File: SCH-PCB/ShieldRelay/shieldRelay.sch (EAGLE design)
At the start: 56 parts, among them IC1 LM2596SX-5.0_NOPB, K1 SLA-05VDC-SL-C, K2 SRD-05VDC-SL-C, K3 G3MB-202PL-DC5, K5 G3MB-202PL-DC5, K6 SRD-05VDC-SL-C, Q1 MMST2222A-7-F, Q2 MMST2222A-7-F, Q3 MMST2222A-7-F, Q4 MMST2222A-7-F, Q5 MMST2222A-7-F

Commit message: FEAT: update schematic
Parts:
- added GND: (no value), pinhead:PINHD-2X4
- added JP13: (no value), pinhead_mod:PINHD-1X15
- renumbered JP10 to VIN, JP7 to VCC_SELECT, JP8 to VCC, JP9 to GND_
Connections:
- net GND: now also GND.1, GND.2, GND.3, GND.4, GND.5, GND.6, GND.7, GND.8
- net N$17: now also JP13.1
- net N$19: now also JP13.2
- net N$20: now also JP13.3
- net N$21: now also JP13.4
- net N$22: now also JP13.5
- net N$28: now also JP13.6
- net N$29: now also JP13.7
- net N$30: now also JP13.8
- net N$31: now also JP13.9
- net N$32: now also JP13.10
- net N$33: now also JP13.11
- net N$34: now also JP13.12
- net N$35: now also JP13.13
- net N$36: now also JP13.14
- net N$37: now also JP13.15

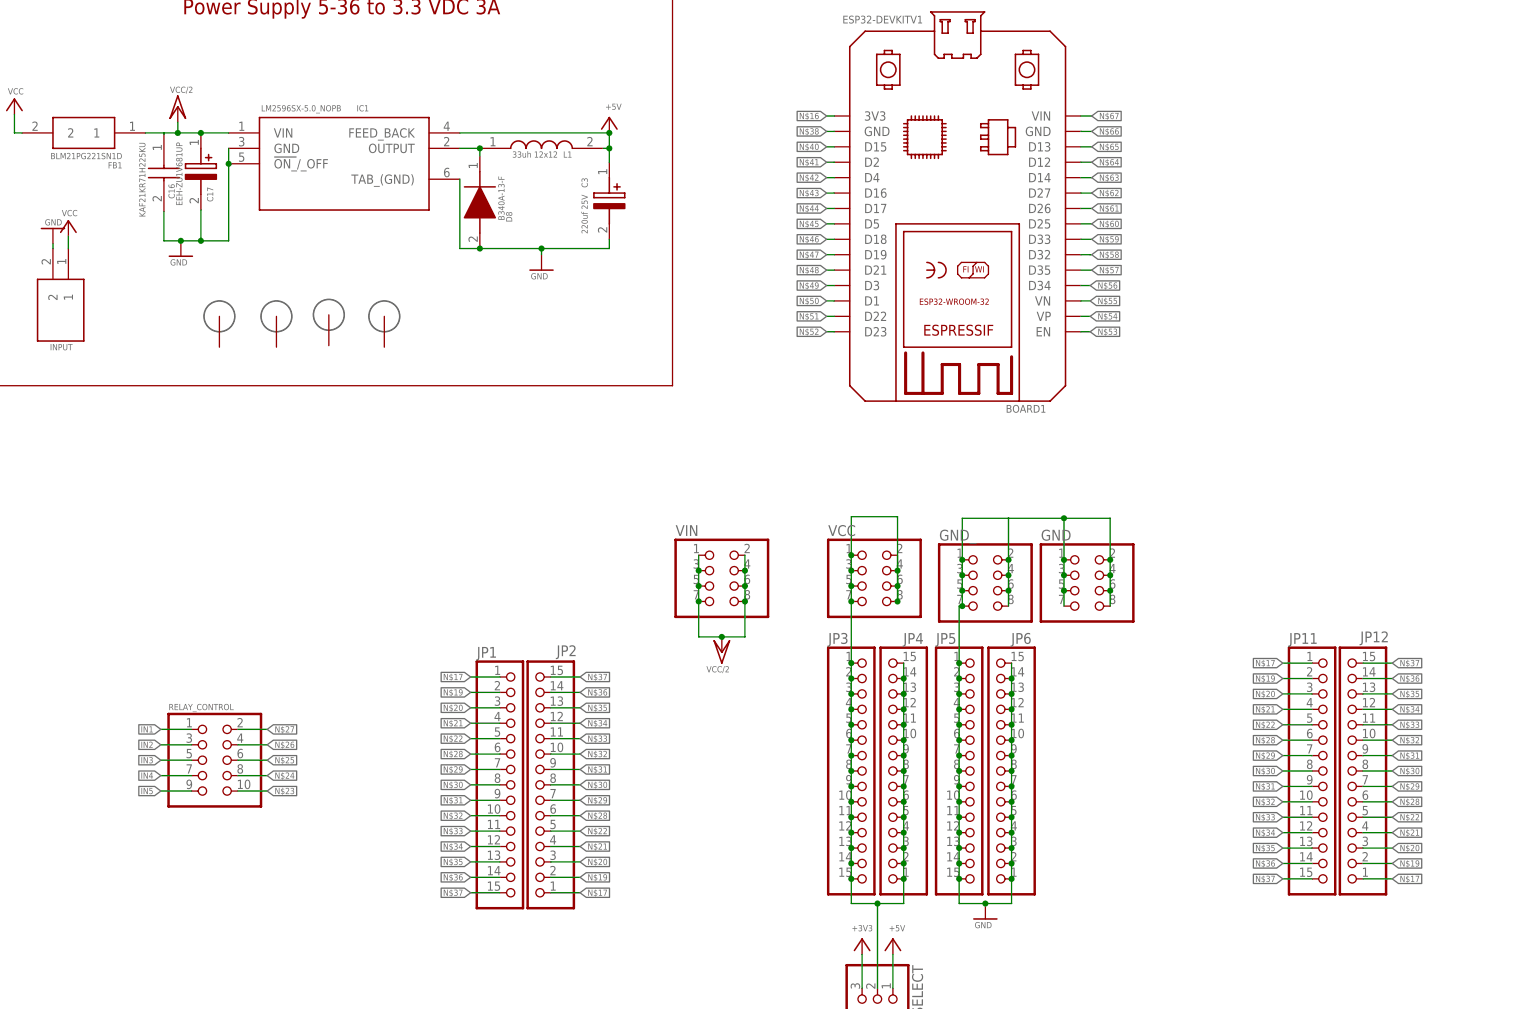
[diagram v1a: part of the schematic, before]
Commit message: FEAT: add 3v3 regulator
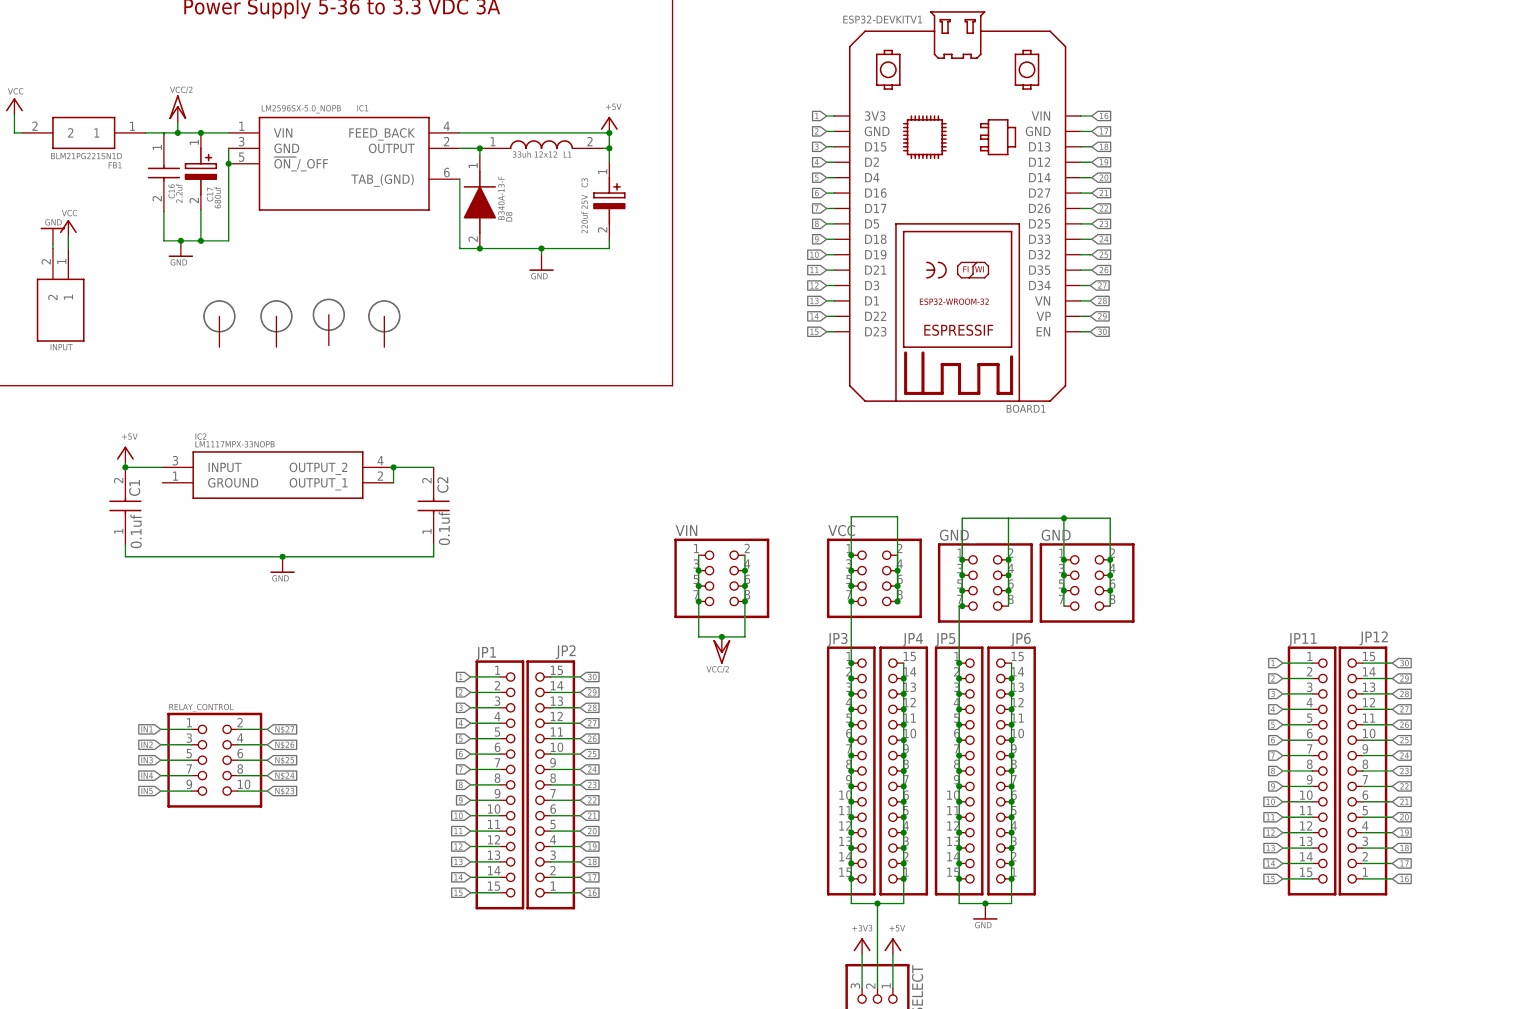
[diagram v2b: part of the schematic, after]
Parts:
- added C1, C2: 0.1uf, KGM15BR71E104KT:KGM15BR71E104KT
- added IC2: LM1117MPX-33NOPB, LM1117MPX-33NOPB:LM1117MPX-33NOPB
- C16: value KAF21KR71H225KU -> 2.2uf
- C17: value EEH-ZU1V681UP -> 680uf
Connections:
- removed net N$16: BOARD1.3V3
- removed net N$40: BOARD1.D15
- removed net N$41: BOARD1.D2
- removed net N$42: BOARD1.D4
- removed net N$43: BOARD1.D16
- removed net N$44: BOARD1.D17
- removed net N$45: BOARD1.D5
- removed net N$46: BOARD1.D18
- removed net N$47: BOARD1.D19
- removed net N$48: BOARD1.D21
- removed net N$49: BOARD1.D3
- removed net N$50: BOARD1.D1
- removed net N$51: BOARD1.D22
- removed net N$52: BOARD1.D23
- removed net N$53: BOARD1.EN
- removed net N$54: BOARD1.VP
- removed net N$55: BOARD1.VN
- removed net N$56: BOARD1.D34
- removed net N$57: BOARD1.D35
- removed net N$58: BOARD1.D32
- removed net N$59: BOARD1.D33
- removed net N$60: BOARD1.D25
- removed net N$61: BOARD1.D26
- removed net N$62: BOARD1.D27
- removed net N$63: BOARD1.D14
- removed net N$64: BOARD1.D12
- removed net N$65: BOARD1.D13
- removed net N$66: BOARD1.GND
- removed net N$67: BOARD1.VIN
- new net 1: BOARD1.3V3, JP1.1, JP11.1
- new net 10: BOARD1.D19, JP1.10, JP11.10
- new net 11: BOARD1.D21, JP1.11, JP11.11
- new net 12: BOARD1.D3, JP1.12, JP11.12
- new net 13: BOARD1.D1, JP1.13, JP11.13
- new net 14: BOARD1.D22, JP1.14, JP11.14
- new net 15: BOARD1.D23, JP1.15, JP11.15
- new net 16: BOARD1.VIN, JP12.1, JP2.1
- new net 17: BOARD1.GND, JP12.2, JP2.2
- new net 18: BOARD1.D13, JP12.3, JP2.3
- new net 19: BOARD1.D12, JP12.4, JP2.4
- new net 2: BOARD1.GND@1, JP1.2, JP11.2
- new net 20: BOARD1.D14, JP12.5, JP2.5
- new net 21: BOARD1.D27, JP12.6, JP2.6
- new net 22: BOARD1.D26, JP12.7, JP2.7
- new net 23: BOARD1.D25, JP12.8, JP2.8
- new net 24: BOARD1.D33, JP12.9, JP2.9
- new net 25: BOARD1.D32, JP12.10, JP2.10
- new net 26: BOARD1.D35, JP12.11, JP2.11
- new net 27: BOARD1.D34, JP12.12, JP2.12
- new net 28: BOARD1.VN, JP12.13, JP2.13
- new net 29: BOARD1.VP, JP12.14, JP2.14
- new net 3: BOARD1.D15, JP1.3, JP11.3
- new net 30: BOARD1.EN, JP12.15, JP2.15
- new net 4: BOARD1.D2, JP1.4, JP11.4
- new net 5: BOARD1.D4, JP1.5, JP11.5
- new net 6: BOARD1.D16, JP1.6, JP11.6
- new net 7: BOARD1.D17, JP1.7, JP11.7
- new net 8: BOARD1.D5, JP1.8, JP11.8
- new net 9: BOARD1.D18, JP1.9, JP11.9
- net +5V: now also C1.2, IC2.INPUT
- net GND: now also C1.1, C2.1
- net N$17: no longer JP1.1, JP11.1, JP12.1, JP2.1
- net N$19: no longer JP1.2, JP11.2, JP12.2, JP2.2
- net N$20: no longer JP1.3, JP11.3, JP12.3, JP2.3
- net N$21: no longer JP1.4, JP11.4, JP12.4, JP2.4
- net N$22: no longer JP1.5, JP11.5, JP12.5, JP2.5
- net N$28: no longer JP1.6, JP11.6, JP12.6, JP2.6
- net N$29: no longer JP1.7, JP11.7, JP12.7, JP2.7
- net N$30: no longer JP1.8, JP11.8, JP12.8, JP2.8
- net N$31: no longer JP1.9, JP11.9, JP12.9, JP2.9
- net N$32: no longer JP1.10, JP11.10, JP12.10, JP2.10
- net N$33: no longer JP1.11, JP11.11, JP12.11, JP2.11
- net N$34: no longer JP1.12, JP11.12, JP12.12, JP2.12
- net N$35: no longer JP1.13, JP11.13, JP12.13, JP2.13
- net N$36: no longer JP1.14, JP11.14, JP12.14, JP2.14
- net N$37: no longer JP1.15, JP11.15, JP12.15, JP2.15
- net N$38: now also C2.2, IC2.OUTPUT_1, IC2.OUTPUT_2; no longer BOARD1.GND@1

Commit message: FEAT: update board
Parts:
- renumbered BOARD1 to BOARD, GND to GND_1, GND_ to GND_2, LED1 to RL3, LED2 to RL1, LED3 to RL4, LED4 to RL5, LED6 to RL2

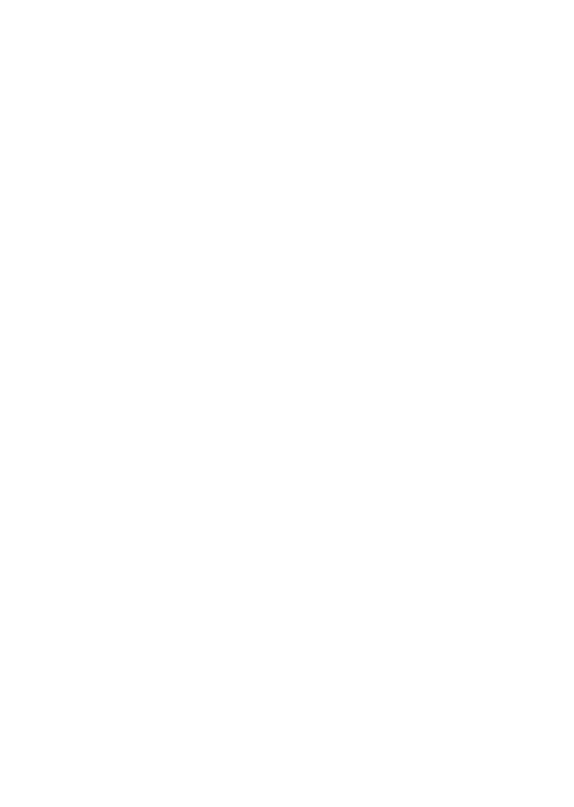
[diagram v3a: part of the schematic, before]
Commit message: FEAT: update terminal block
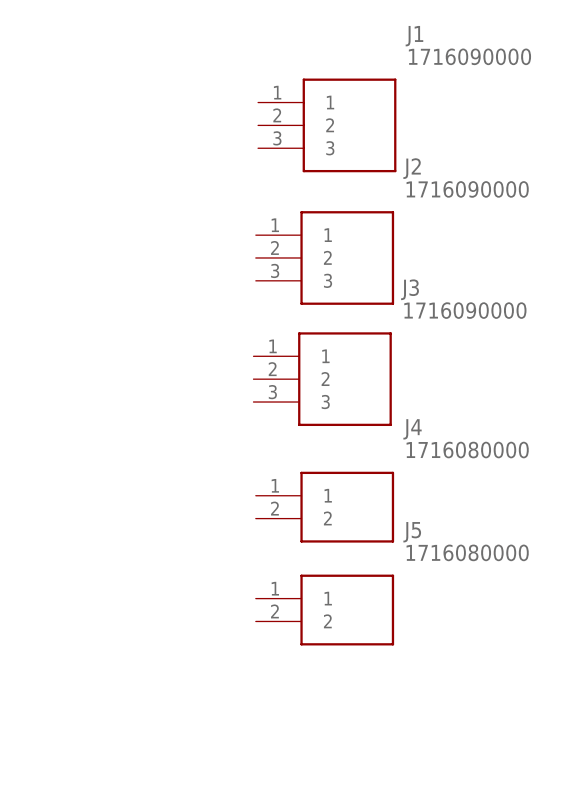
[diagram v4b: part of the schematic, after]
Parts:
- added J1, J2, J3: 1716090000, 1716090000:1716090000
- added J4, J5: 1716080000, 1716080000:1716080000
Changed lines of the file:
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@@
 <part name="GND10" library="supply1" library_urn="urn:adsk.eagle:library:371" deviceset="GND" device=""/>
 <part name="P+12" library="supply1" library_urn="urn:adsk.eagle:library:371" deviceset="+5V" device=""/>
+<part name="J1" library="1716090000" deviceset="1716090000" device=""/>
+<part name="J2" library="1716090000" deviceset="1716090000" device=""/>
+<part name="J3" library="1716090000" deviceset="1716090000" device=""/>
+<part name="J4" library="1716080000" deviceset="1716080000" device=""/>
+<part name="J5" library="1716080000" deviceset="1716080000" device=""/>
 </parts>
 <sheets>
@@
 <attribute name="VALUE" x="300.99" y="105.664" size="1.016" layer="96" rot="R180"/>
 </instance>
+<instance part="J1" gate="G$1" x="526.542" y="176.022" smashed="yes">
+<attribute name="NAME" x="543.052" y="183.642" size="1.778" layer="95" align="center-left"/>
+<attribute name="VALUE" x="543.052" y="181.102" size="1.778" layer="96" align="center-left"/>
+</instance>
+<instance part="J2" gate="G$1" x="526.288" y="161.29" smashed="yes">
+<attribute name="NAME" x="542.798" y="168.91" size="1.778" layer="95" align="center-left"/>
+<attribute name="VALUE" x="542.798" y="166.37" size="1.778" layer="96" align="center-left"/>
+</instance>
+<instance part="J3" gate="G$1" x="526.034" y="147.828" smashed="yes">
+<attribute name="NAME" x="542.544" y="155.448" size="1.778" layer="95" align="center-left"/>
+<attribute name="VALUE" x="542.544" y="152.908" size="1.778" layer="96" align="center-left"/>
+</instance>
+<instance part="J4" gate="G$1" x="526.288" y="132.334" smashed="yes">
+<attribute name="NAME" x="542.798" y="139.954" size="1.778" layer="95" align="center-left"/>
+<attribute name="VALUE" x="542.798" y="137.414" size="1.778" layer="96" align="center-left"/>
+</instance>
+<instance part="J5" gate="G$1" x="526.288" y="120.904" smashed="yes">
+<attribute name="NAME" x="542.798" y="128.524" size="1.778" layer="95" align="center-left"/>
+<attribute name="VALUE" x="542.798" y="125.984" size="1.778" layer="96" align="center-left"/>
+</instance>
 </instances>

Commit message: DOC: UPDATE SCHEMATIC, BOARD AND ADD PDF
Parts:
- removed J1, J2, J3: 1716090000, 1716090000:1716090000
- removed J4, J5: 1716080000, 1716080000:1716080000
- removed JP1, JP2, JP3, JP4, JP5, JP6: (no value), pinhead_mod:PINHD-1X15
- added GND_3, GND_4, SIGNAL_3, SIGNAL_4, VCC_3, VCC_4: (no value), pinhead_mod:PINHD-1X15
- added RELAY1, RELAY2, RELAY3: 1716090000, 1716090000:1716090000
- added RELAY4, RELAY5: 1716080000, 1716080000:1716080000
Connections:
- removed net 16: BOARD.VIN, JP12.1, JP2.1
- removed net 17: BOARD.GND, JP12.2, JP2.2
- removed net N$17: JP13.1
- removed net N$19: JP13.2
- removed net N$20: JP13.3
- removed net N$21: JP13.4
- removed net N$22: JP13.5
- removed net N$28: JP13.6
- removed net N$29: JP13.7
- removed net N$30: JP13.8
- removed net N$31: JP13.9
- removed net N$32: JP13.10
- removed net N$33: JP13.11
- removed net N$34: JP13.12
- removed net N$35: JP13.13
- removed net N$36: JP13.14
- removed net N$37: JP13.15
- new net COM1: K2.COM, RELAY2.2
- new net COM2: K1.COM_1, K1.COM_2, RELAY1.2
- new net COM3: K6.COM, RELAY3.2
- new net COM4: K3.LOAD_1, RELAY5.1
- new net COM5: K5.LOAD_1, RELAY4.1
- new net NC1: K2.NC, RELAY2.1
- new net NC2: K1.NC, RELAY1.1
- new net NC3: K6.NC, RELAY3.1
- new net NO1: K2.NO, RELAY2.3
- new net NO2: K1.NO, RELAY1.3
- new net NO3: K6.NO, RELAY3.3
- new net NO4: K3.LOAD_2, RELAY5.2
- new net NO5: K5.LOAD_2, RELAY4.2
- net +5V: now also BOARD.VIN, JP12.1, JP13.1, SIGNAL_3.1
- net 1: now also SIGNAL_4.1; no longer JP1.1
- net 10: now also SIGNAL_4.10; no longer JP1.10
- net 11: now also SIGNAL_4.11; no longer JP1.11
- net 12: now also SIGNAL_4.12; no longer JP1.12
- net 13: now also SIGNAL_4.13; no longer JP1.13
- net 14: now also SIGNAL_4.14; no longer JP1.14
- net 15: now also SIGNAL_4.15; no longer JP1.15
- net 18: now also JP13.3, SIGNAL_3.3; no longer JP2.3
- net 19: now also JP13.4, SIGNAL_3.4; no longer JP2.4
- net 2: now also SIGNAL_4.2; no longer JP1.2
- net 20: now also JP13.5, SIGNAL_3.5; no longer JP2.5
- net 21: now also JP13.6, SIGNAL_3.6; no longer JP2.6
- net 22: now also JP13.7, SIGNAL_3.7; no longer JP2.7
- net 23: now also JP13.8, SIGNAL_3.8; no longer JP2.8
- net 24: now also JP13.9, SIGNAL_3.9; no longer JP2.9
- net 25: now also JP13.10, SIGNAL_3.10; no longer JP2.10
- net 26: now also JP13.11, SIGNAL_3.11; no longer JP2.11
- net 27: now also JP13.12, SIGNAL_3.12; no longer JP2.12
- net 28: now also JP13.13, SIGNAL_3.13; no longer JP2.13
- net 29: now also JP13.14, SIGNAL_3.14; no longer JP2.14
- net 3: now also SIGNAL_4.3; no longer JP1.3
- net 30: now also JP13.15, SIGNAL_3.15; no longer JP2.15
- net 4: now also SIGNAL_4.4; no longer JP1.4
- net 5: now also SIGNAL_4.5; no longer JP1.5
- net 6: now also SIGNAL_4.6; no longer JP1.6
- net 7: now also SIGNAL_4.7; no longer JP1.7
- net 8: now also SIGNAL_4.8; no longer JP1.8
- net 9: now also SIGNAL_4.9; no longer JP1.9
- net GND: now also BOARD.GND, GND_3.1, GND_3.10, GND_3.11, GND_3.12, GND_3.13, GND_3.14, GND_3.15, GND_3.2, GND_3.3, GND_3.4, GND_3.5, GND_3.6, GND_3.7, GND_3.8, GND_3.9, GND_4.1, GND_4.10, GND_4.11, GND_4.12, GND_4.13, GND_4.14, GND_4.15, GND_4.2, GND_4.3, GND_4.4, GND_4.5, GND_4.6, GND_4.7, GND_4.8, GND_4.9, JP12.2, JP13.2, SIGNAL_3.2; no longer JP5.1, JP5.10, JP5.11, JP5.12, JP5.13, JP5.14, JP5.15, JP5.2, JP5.3, JP5.4, JP5.5, JP5.6, JP5.7, JP5.8, JP5.9, JP6.1, JP6.10, JP6.11, JP6.12, JP6.13, JP6.14, JP6.15, JP6.2, JP6.3, JP6.4, JP6.5, JP6.6, JP6.7, JP6.8, JP6.9
- net N$39: now also VCC_3.1, VCC_3.10, VCC_3.11, VCC_3.12, VCC_3.13, VCC_3.14, VCC_3.15, VCC_3.2, VCC_3.3, VCC_3.4, VCC_3.5, VCC_3.6, VCC_3.7, VCC_3.8, VCC_3.9, VCC_4.1, VCC_4.10, VCC_4.11, VCC_4.12, VCC_4.13, VCC_4.14, VCC_4.15, VCC_4.2, VCC_4.3, VCC_4.4, VCC_4.5, VCC_4.6, VCC_4.7, VCC_4.8, VCC_4.9; no longer JP3.1, JP3.10, JP3.11, JP3.12, JP3.13, JP3.14, JP3.15, JP3.2, JP3.3, JP3.4, JP3.5, JP3.6, JP3.7, JP3.8, JP3.9, JP4.1, JP4.10, JP4.11, JP4.12, JP4.13, JP4.14, JP4.15, JP4.2, JP4.3, JP4.4, JP4.5, JP4.6, JP4.7, JP4.8, JP4.9
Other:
- note added: "5 X RELAY"
- note added: "ESP32"
- note added: "JUARENDRA R."
- note added: "PIN HEADER"
- note added: "PIN HEADER AND ESP32"
- note added: "Power Supply 5-36 to 5V VDC 3A"
- note added: "Power Supply 5VDCX to 3.3 VDC 1A"
- note added: "RELAY AND POWER SUPPLY"
- note removed: "Power Supply 5-36 to 3.3 VDC 3A"

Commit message: FEAT: add 3D model
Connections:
- net +5V: now also K1.COIL_2; no longer K1.COIL_1
- net N$8: now also K1.COIL_1; no longer K1.COIL_2
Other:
- moved on the sheet: K1
